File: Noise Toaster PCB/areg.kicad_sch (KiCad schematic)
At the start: 14 parts, among them J3 AREG, Q1 2N3906, Q9 2N5457, U2 LM324

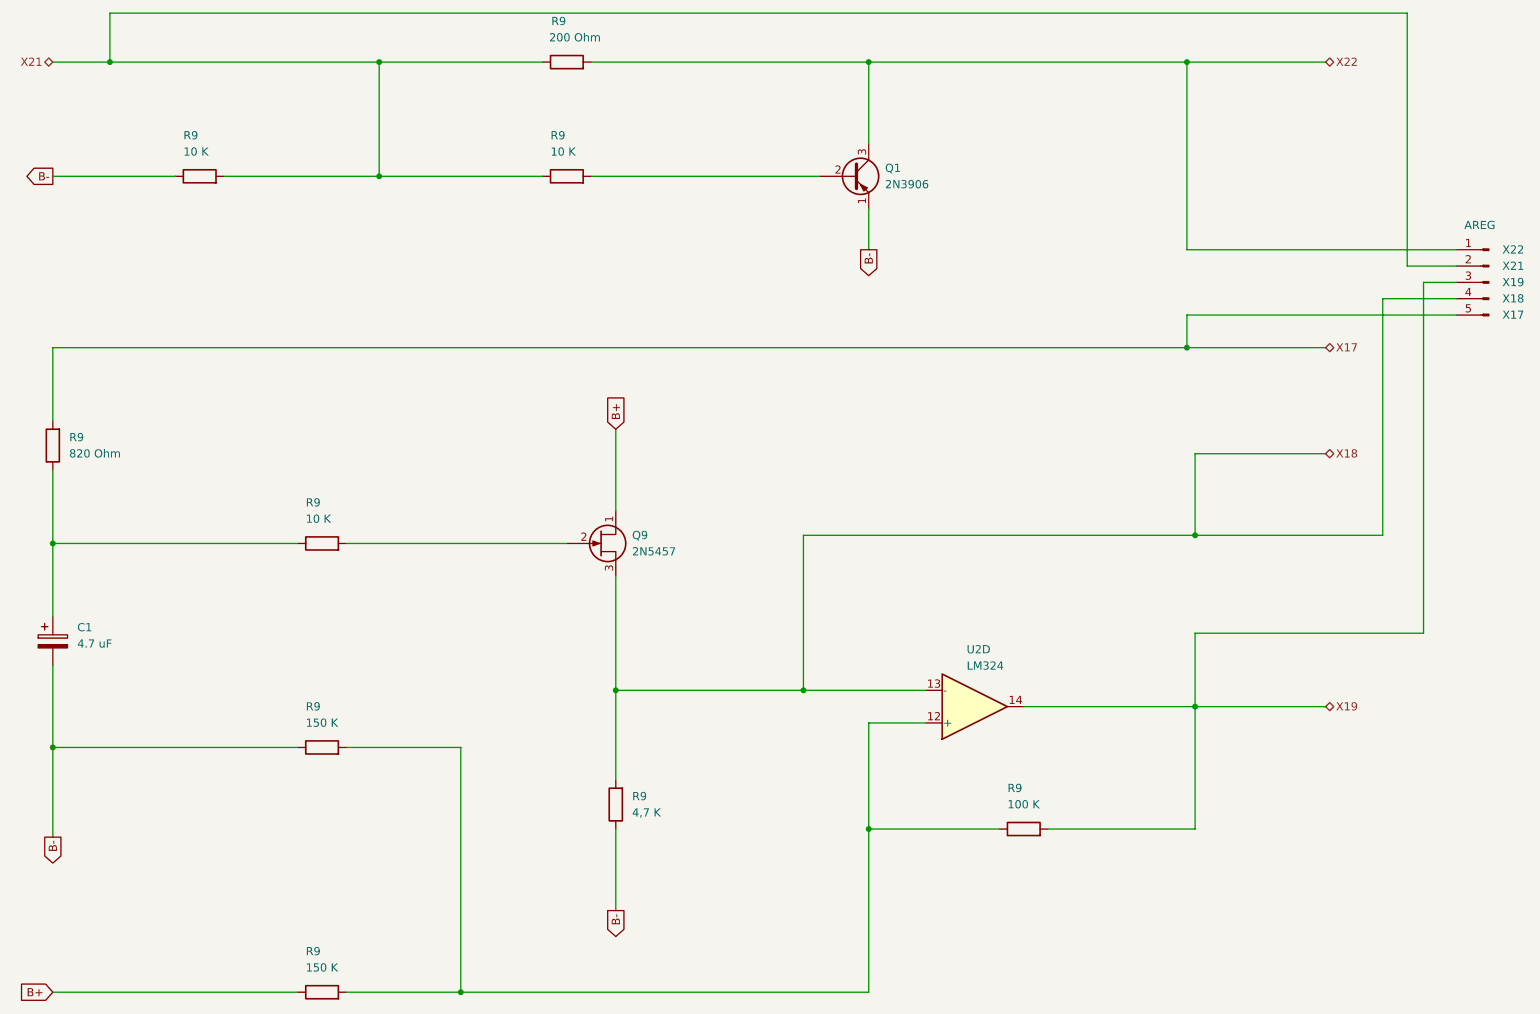
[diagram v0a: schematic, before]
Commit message: added front panel pcb
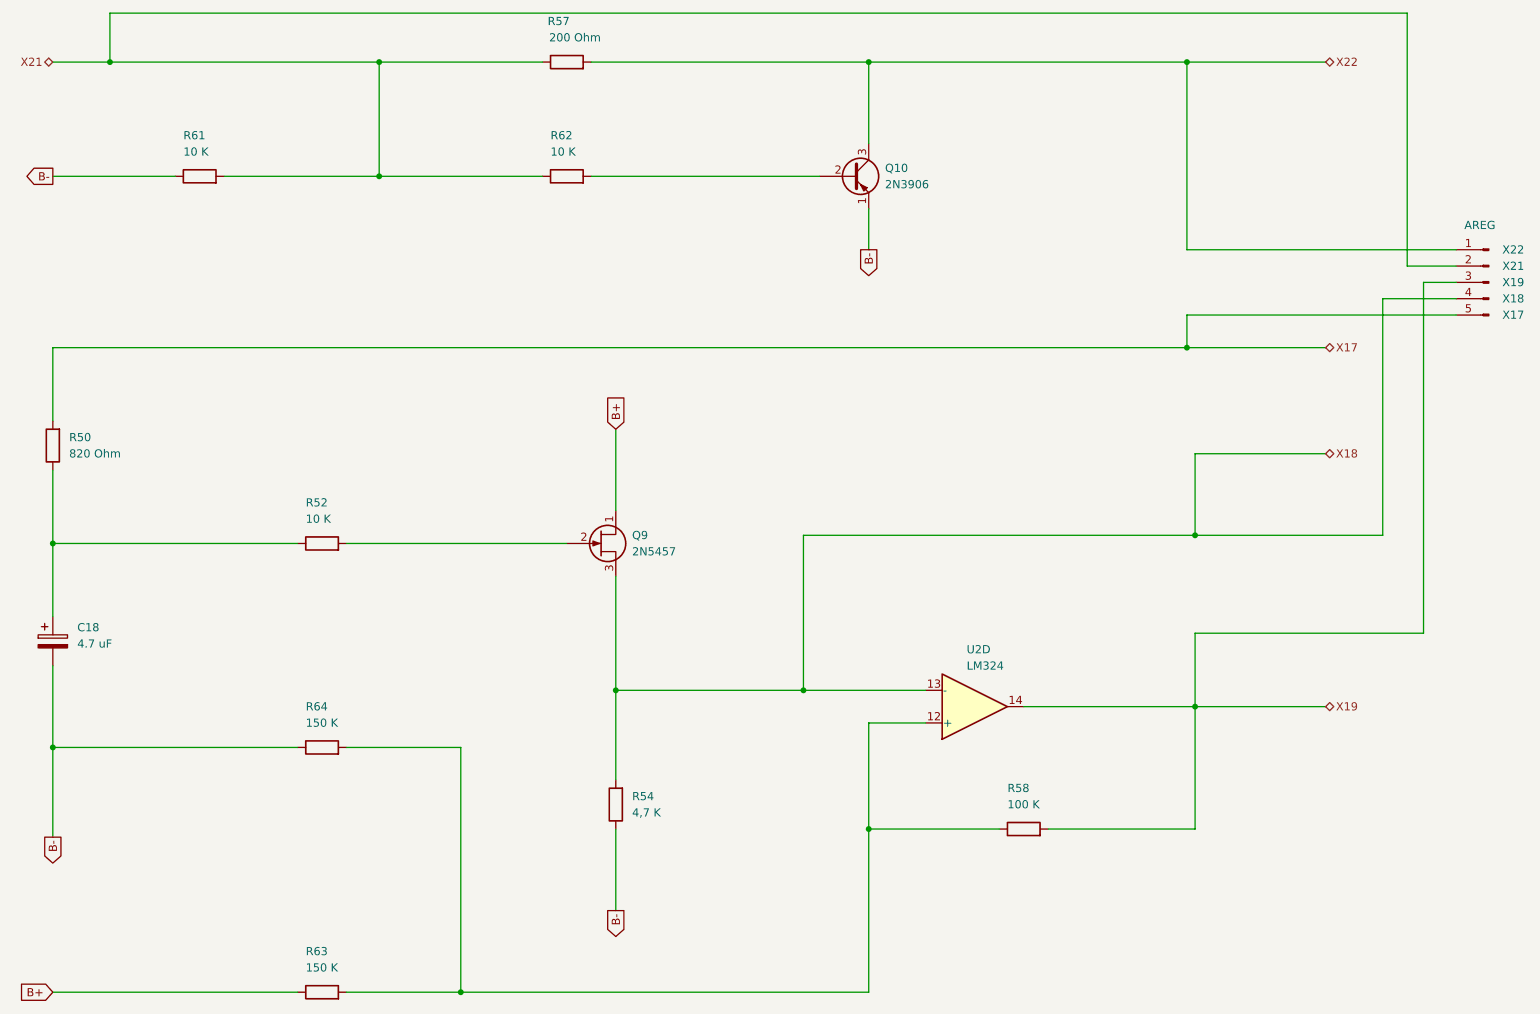
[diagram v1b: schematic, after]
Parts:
- renumbered C1 to C18, Q1 to Q10, R9 to R50, R9 to R52, R9 to R54, R9 to R57, R9 to R58, R9 to R61, R9 to R62, R9 to R63, R9 to R64
